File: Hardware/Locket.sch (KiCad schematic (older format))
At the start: 66 parts, among them Q1 LED_RGB 5050, Q2 IRLML9303, Q3 IRLML9303, SW1 SWITCH, SW2 BUTTON, SW3 DIPx4

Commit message: + Accelerometer + Proceeding with antenna & PCB
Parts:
- added C24, C9: 0.1u, Capacitors:SMD_0603, symbol C
- added C7: 10u, Capacitors:SMD_0805, symbol C
- added DD3: MMA8452Q, QFN:QFN16_5_3, symbol MMA8452Q
- added R10, R11: 4k7, symbol R
- F1, F2, F3, F4: footprint (none) -> Resistors:SMD_0603_FUSE
- SW3: footprint (none) -> Switches:DIP_SMD_X4
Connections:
- net +BATT: now also C7.1, C9.1, DD3.1 (VDDIO), DD3.14 (VDD), R10.1, R11.2
- net DS1: now also DD1.29 (MCO/CK1/PA8); no longer DD1.20 (PB2/BOOT1)
- net DS2: now also DD1.32 (MISO1/USBDM/PA11); no longer DD1.21 (PB10/SCL2/TX3/T2C3)
- net DS3: now also DD1.33 (MOSI1/USBDP/PA12); no longer DD1.22 (PB11/SDA2/RX3/T2C4)
- net DS4: now also DD1.38 (JTDI/T2C1ETR/PA15); no longer DD1.25 (PB12/CK3/T10C1/ADC18)
- net GND: now also C24.2, C7.2, C9.2, DD3.10 (GND), DD3.12 (GND), DD3.5 (GND), DD3.7 (SA0); no longer R7.2
- net GNDPWR: now also R7.2
- net P_SCL: now also DD1.42 (PB6/SCL1/T4C1/TX1); no longer DD1.45 (PB8/SCL1/T4C3/T10C1)
- net P_SDA: now also DD1.43 (PB7/SDA1/T4C2/RX1); no longer DD1.46 (PB9/SDA1/T4C4/T11C1)
- net PeriphPwr: now also DD1.46 (PB9/SDA1/T4C4/T11C1); no longer DD1.43 (PB7/SDA1/T4C2/RX1)
- net Vibro: now also DD1.45 (PB8/SCL1/T4C3/T10C1); no longer DD1.42 (PB6/SCL1/T4C1/TX1)
- new net: C24.1, DD3.2 (BYP)
- new net ACC_INT1: DD3.11 (INT1)
- new net I2C_SCL: DD1.21 (PB10/SCL2/TX3/T2C3), DD3.4 (SCL), R10.2
- new net I2C_SDA: DD1.22 (PB11/SDA2/RX3/T2C4), DD3.6 (SDA), R11.1
- no-connect marks 11 -> 10
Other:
- note added: "Accelerometer\nI2C addr = 0x1C"
- moved on the sheet: ANT1, BLN1, C1, C10, C11, C12, C13, C14, C15, C16, C17, C18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

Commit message: + Additional footprints for motor and switch
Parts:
- added M1: MOTOR_PAD, Installations:MOTOR_KHN4NX, symbol MOTOR_PAD
- added SW4: SWITCH, Switches:SW_SS-1P2T, symbol SWITCH
- F1, F2, F3, F4: footprint Resistors:SMD_0603_FUSE -> Resistors:RES_0603_FUSE
- R1, R2, R3, R4, R5, R6, R7, R8, R9: footprint Resistors:SMD_0603 -> Resistors:RES_0603
- R10, R11: footprint (none) -> Resistors:RES_0603
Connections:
- net +BATT: now also SW4.1
- net BAT_IN: now also SW4.2
- net GNDPWR: now also M1.1 (+), M1.PAD (GND)
- net VibroOut: now also M1.2 (-)
- no-connect marks 10 -> 11
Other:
- note added: "Choose one of two footprints"
- note added: "Choose one or another motor"
- moved on the sheet: BZ1, D2, Q2, Q3, SW1, XL2, XL6

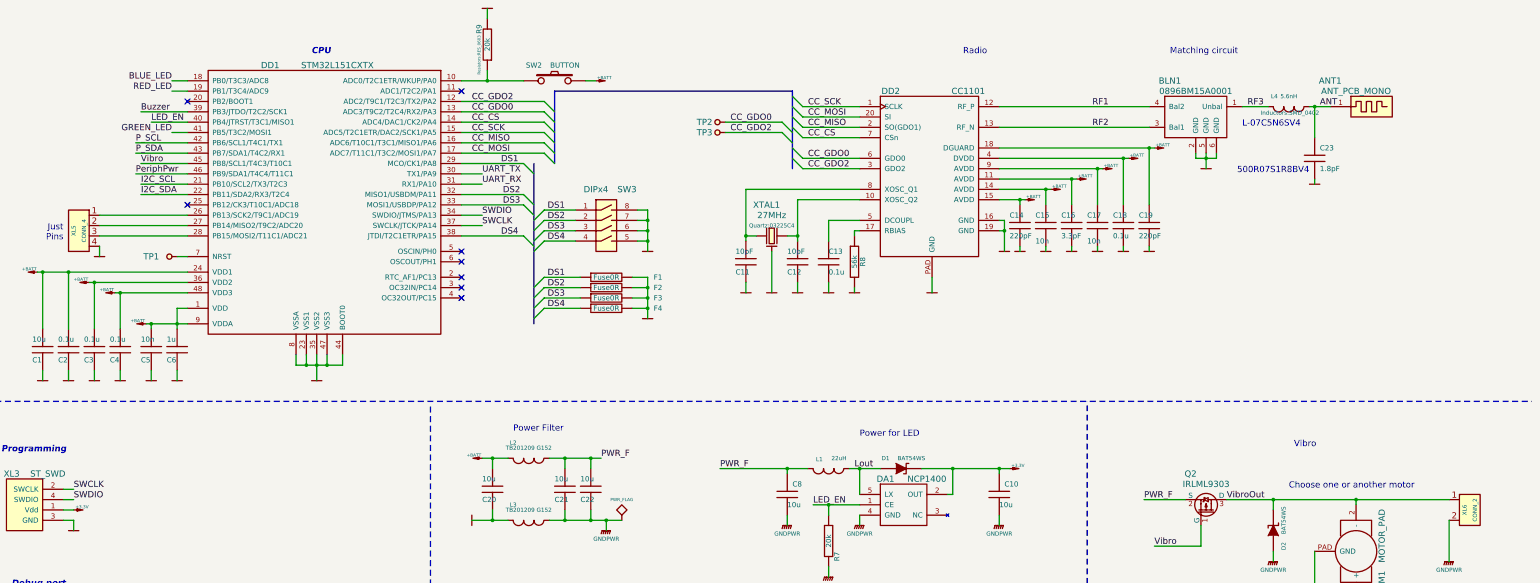
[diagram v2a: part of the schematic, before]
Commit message: + PCB routed, but DRC not tested
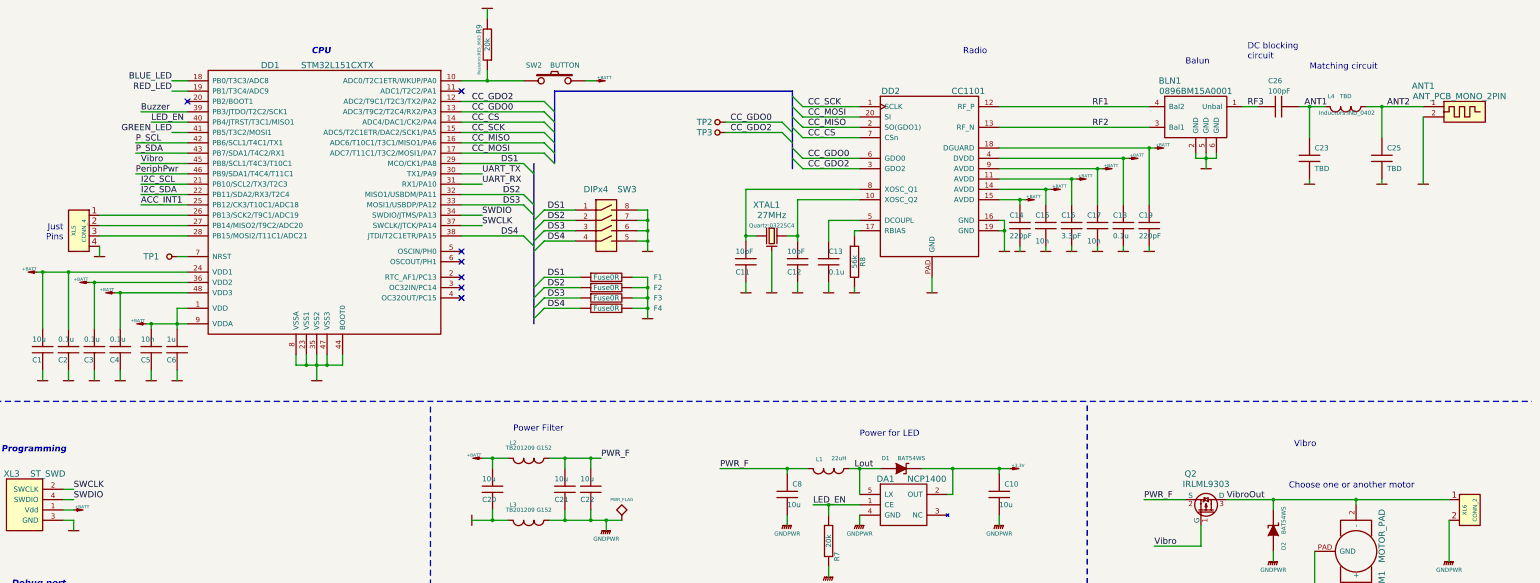
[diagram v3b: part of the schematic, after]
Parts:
- removed ANT1: ANT_PCB_MONO, Radio:ANT_868_SEIDHE, symbol ANT_PCB_MONO
- added ANT1: ANT_PCB_MONO_2PIN, Radio:ANT_868_ROUND_F, symbol ANT_PCB_MONO_2PIN
- added C25: TBD, Capacitors:CAP_0402, symbol C
- added C26: 100pF, Capacitors:CAP_0402, symbol C
- C1, C10, C20, C21, C22, C7, C8: footprint Capacitors:SMD_0805 -> Capacitors:CAP_0805
- C11, C12, C13, C14, C15, C16, C17, C18, C19, C2, C24, C3, C4, C5, C6, C9: footprint Capacitors:SMD_0603 -> Capacitors:CAP_0603
- C23: value 1.8pF -> TBD; footprint Capacitors:SMD_0402 -> Capacitors:CAP_0402
- L1: footprint Inductors:SMD_1210_LQH32C -> Inductors:IND_1210_LQH32C
- L2, L3: footprint Inductors:SMD_0805 -> Inductors:IND_0805
- L4: value 5.6nH -> TBD; footprint Inductors:SMD_0402 -> Inductors:IND_0402
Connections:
- net +3.3V: no longer XL3.1 (Vdd)
- net +BATT: now also XL3.1 (Vdd)
- net ACC_INT1: now also DD1.25 (PB12/CK3/T10C1/ADC18)
- net GND: now also ANT1.2, C25.2
- net RF3: now also C26.2; no longer L4.2
- net ANT renamed ANT1
- net ANT1: now also L4.2, C26.1; no longer L4.1
- new net ANT2: ANT1.1, C25.1, L4.1
- no-connect marks 11 -> 10
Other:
- note added: "Balun"
- note added: "DC blocking \ncircuit"
- note removed: "500R07S1R8BV4"
- note removed: "L-07C5N6SV4"
- moved on the sheet: C23, L4

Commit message: + Antenna matched, log doc added
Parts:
- C23: value TBD -> DoNotMount
- C25: value TBD -> 1.5pF
- L4: value TBD -> 33nH
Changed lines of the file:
@@
 P 13950 2350
 F 0 "C23" H 14000 2450 50  0000 L CNN
-F 1 "TBD" H 14000 2250 50  0000 L CNN
+F 1 "DoNotMount" H 14000 2250 50  0000 L CNN
 F 2 "Capacitors:CAP_0402" H 13950 2350 60  0001 C CNN
 F 3 "" H 13950 2350 60  0001 C CNN
@@
 P 14300 1850
 F 0 "L4" V 14200 1710 40  0000 C CNN
-F 1 "TBD" V 14200 1850 40  0000 C CNN
+F 1 "33nH" V 14200 1850 40  0000 C CNN
 F 2 "Inductors:IND_0402" V 14360 1860 40  0000 C CNN
 F 3 "~" H 14300 1850 60  0000 C CNN
@@
 P 14650 2350
 F 0 "C25" H 14700 2450 50  0000 L CNN
-F 1 "TBD" H 14700 2250 50  0000 L CNN
+F 1 "1.5pF" H 14700 2250 50  0000 L CNN
 F 2 "Capacitors:CAP_0402" H 14650 2350 60  0001 C CNN
 F 3 "" H 14650 2350 60  0001 C CNN
